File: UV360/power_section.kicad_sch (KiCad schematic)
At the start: 25 parts, among them J1 5V, J15 5V-SW, J16 12V-SW, J2 12V-IN, J3 12V-OUT

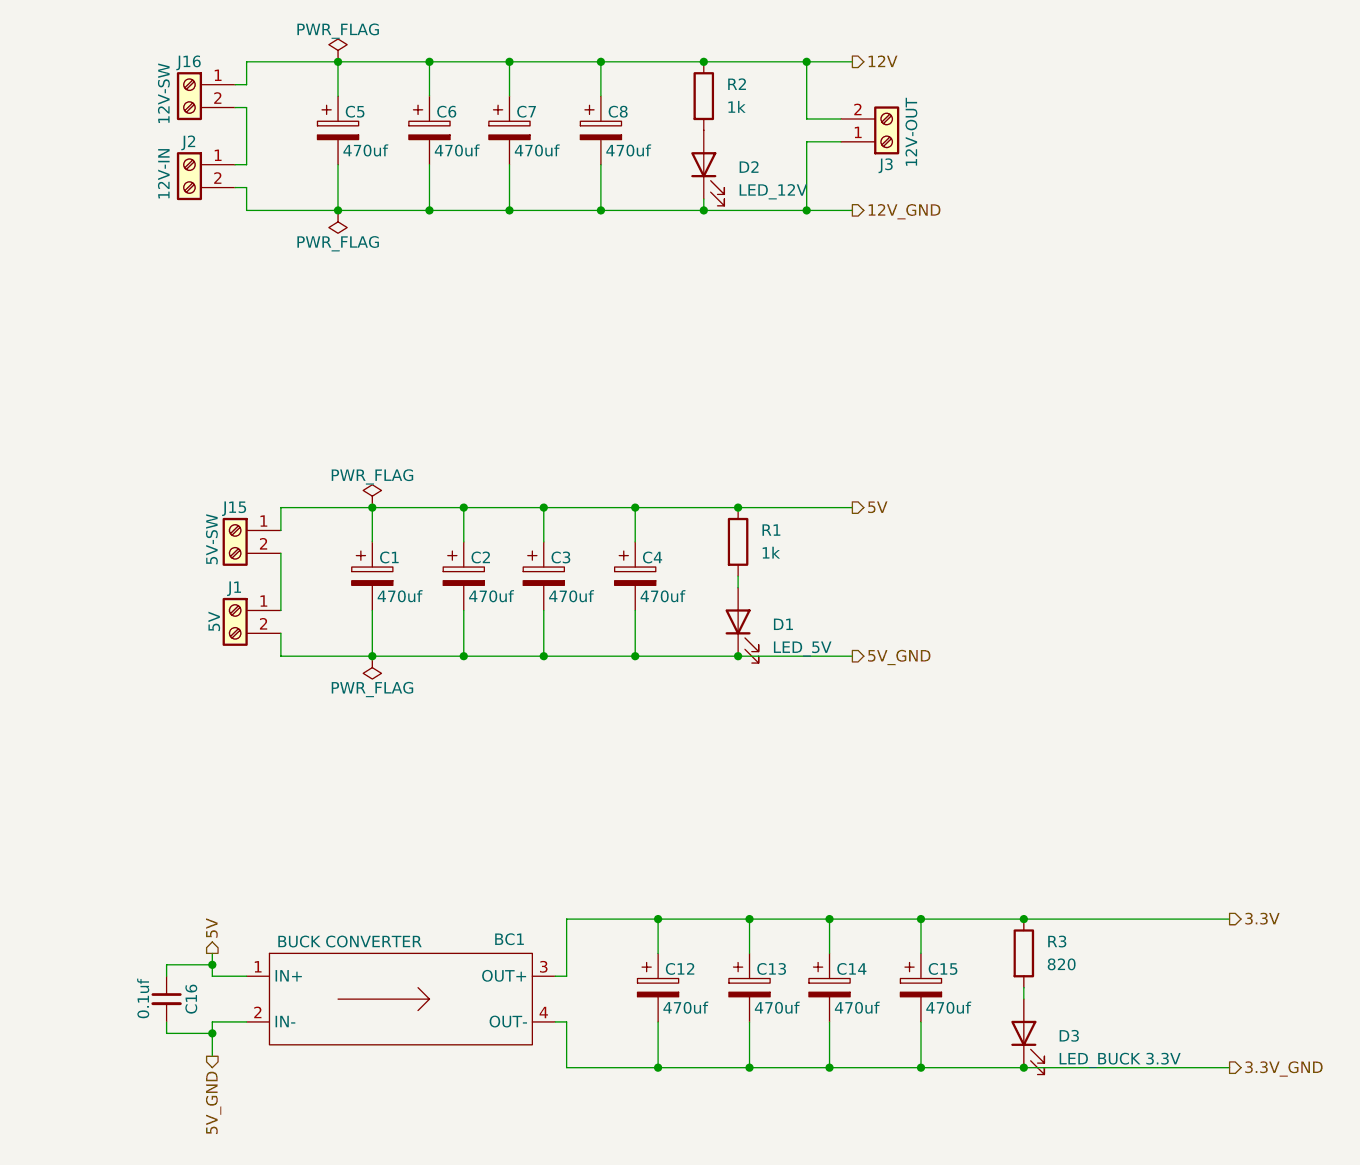
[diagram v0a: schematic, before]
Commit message: Power Section
12v smps in, 7805 regulator, 3.3v buck converter
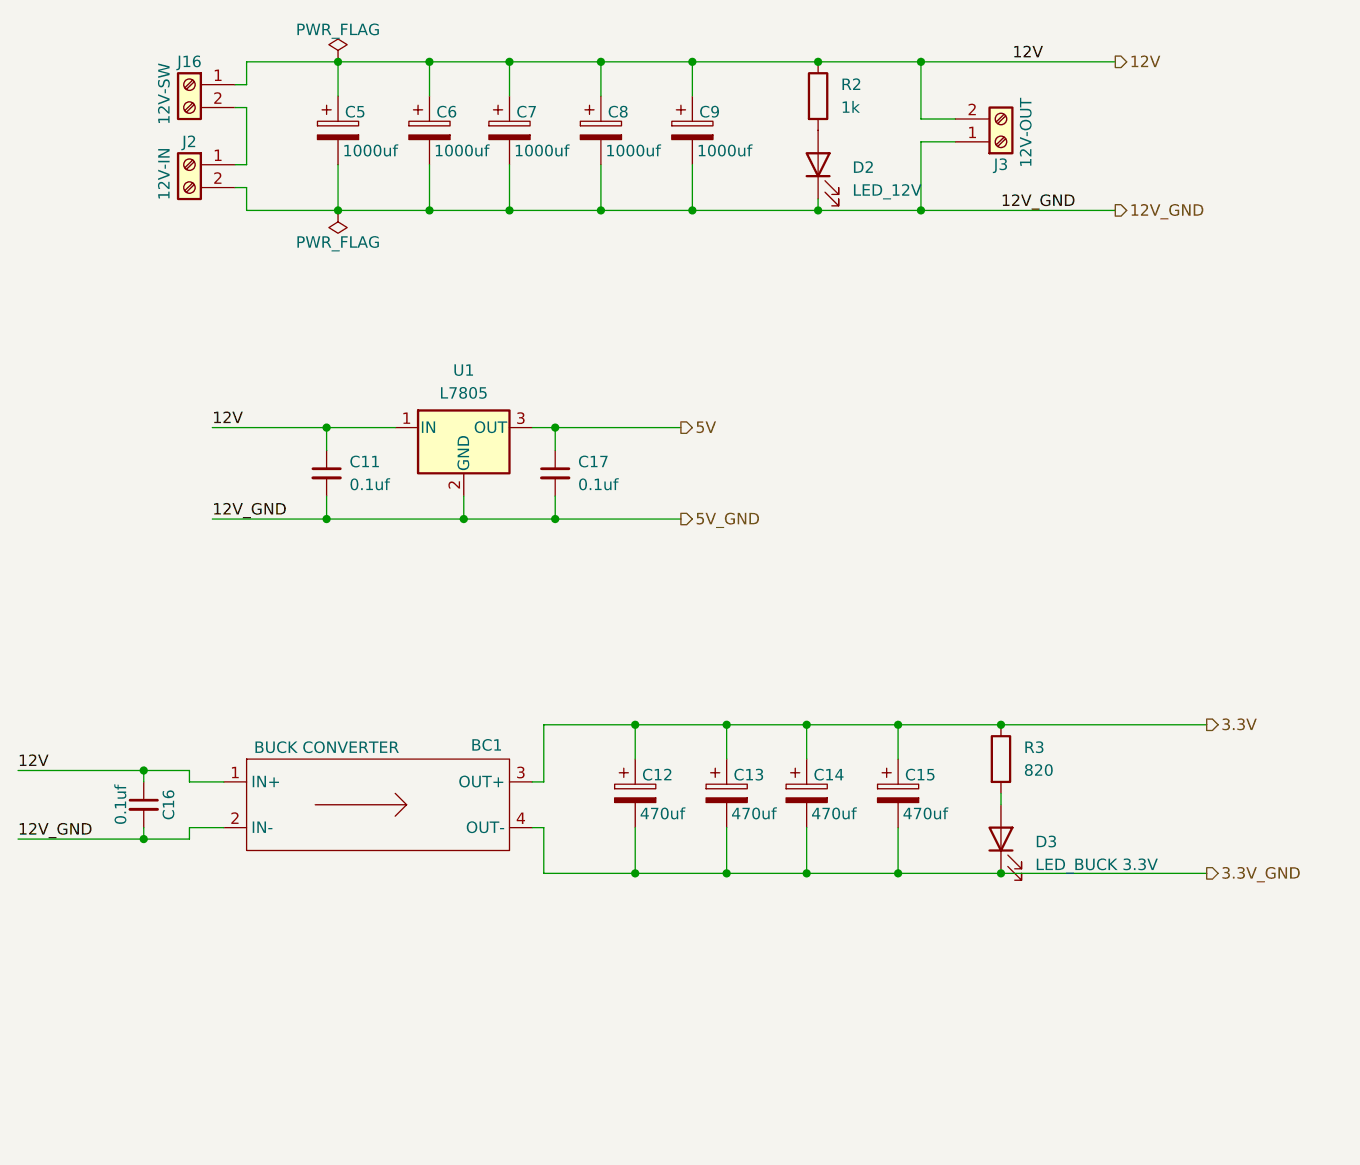
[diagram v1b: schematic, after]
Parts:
- removed C1, C2, C3, C4: 470uf, Capacitor_THT:CP_Radial_D10.0mm_P7.50mm, symbol Device:C_Polarized
- removed D1: LED_5V, LED_THT:LED_D3.0mm, symbol Device:LED
- removed J1: 5V, TerminalBlock_Phoenix:TerminalBlock_Phoenix_MKDS-1,5-2-5.08_1x02_P5.08mm_Horizontal, symbol Connector:Screw_Terminal_01x02
- removed J15: 5V-SW, TerminalBlock_Phoenix:TerminalBlock_Phoenix_MKDS-1,5-2-5.08_1x02_P5.08mm_Horizontal, symbol Connector:Screw_Terminal_01x02
- removed R1: 1k, Resistor_THT:R_Axial_DIN0204_L3.6mm_D1.6mm_P7.62mm_Horizontal, symbol Device:R
- added C11, C17: 0.1uf, symbol Device:C_Small
- added C9: 1000uf, Capacitor_THT:CP_Radial_D10.0mm_P7.50mm, symbol Device:C_Polarized
- added U1: L7805, symbol Regulator_Linear:L7805
- C5, C6, C7, C8: value 470uf -> 1000uf
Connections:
- net 5V_GND is gone; now on net 12V_GND: BC1.2 (IN-), C16.2
- net 12V: now also BC1.1 (IN+), C16.1, C11.1, C9.1, U1.1 (IN)
- net 12V_GND: now also C11.2, C17.2, C9.2, U1.2 (GND)
- net 5V: now also C17.1, U1.3 (OUT); no longer BC1.1 (IN+), C16.1
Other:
- moved on the sheet: BC1, C12, C13, C14, C15, C16, D2, D3, J3, R2, R3
